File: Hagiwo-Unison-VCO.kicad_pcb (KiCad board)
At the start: 2 copper layers, 30 x 100 mm, 50 parts, among them J1 OSC2 VOL, J2 V/OCT, J3 Eurorack, J4 OUT, J5 Display, SW1 Wave, U1 XIAO_RA4M1, U2 AMS1117-5.0, U3 TL072, U4 TL072

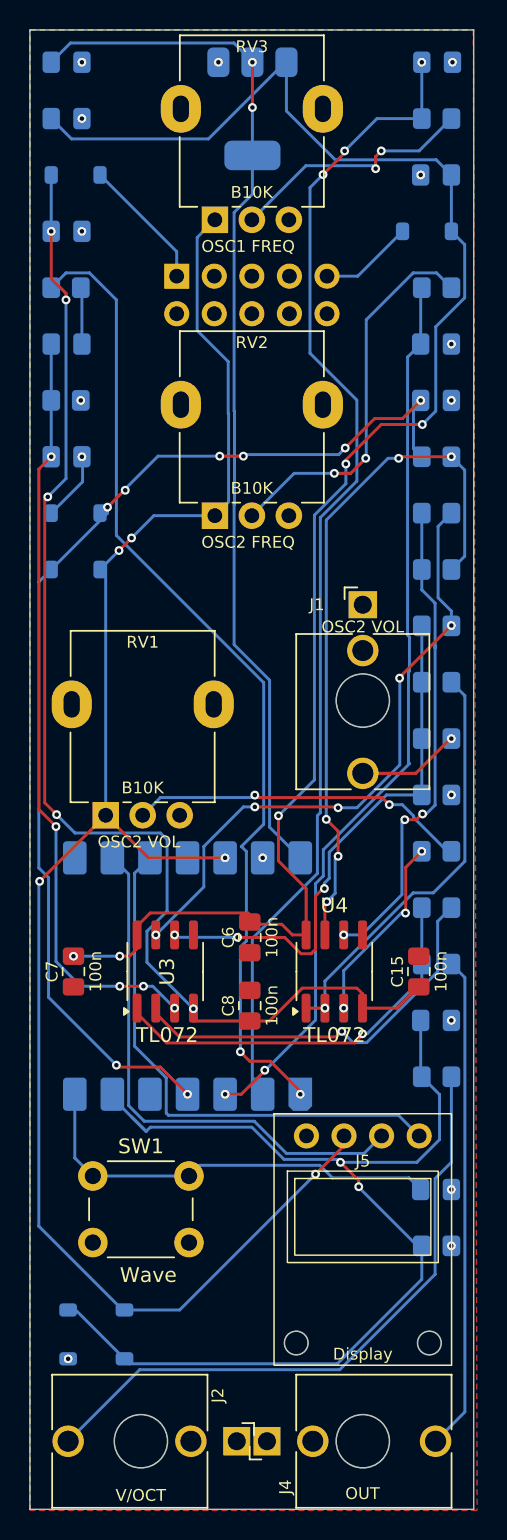
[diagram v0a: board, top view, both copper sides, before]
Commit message: add a pcb front panel
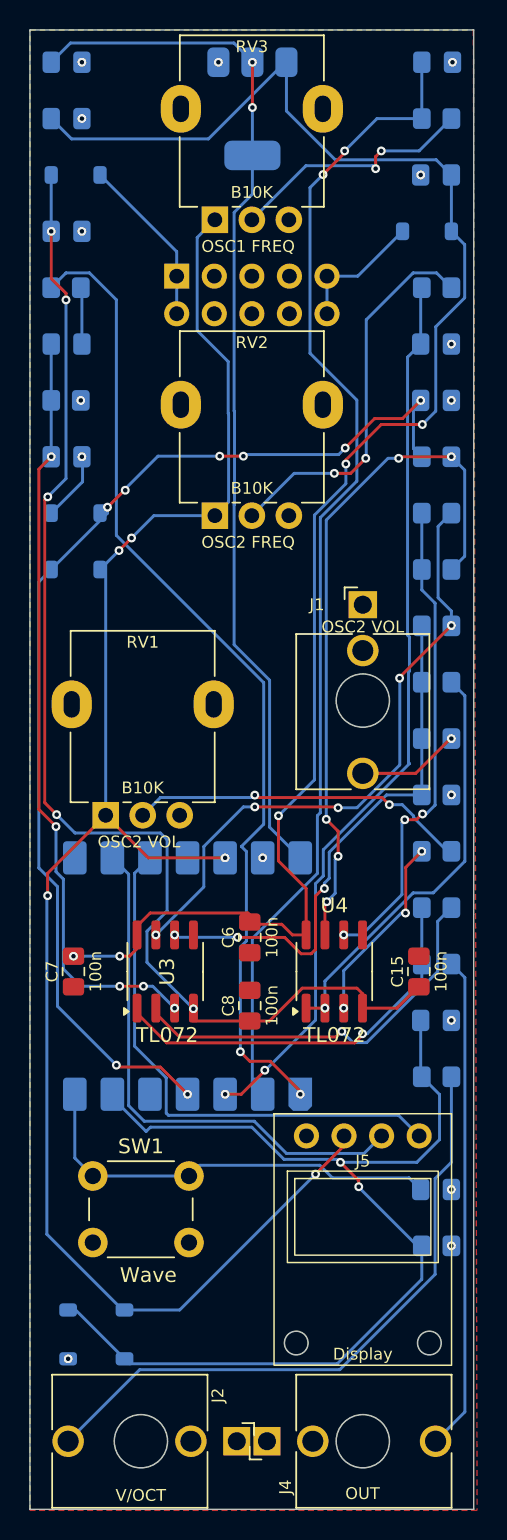
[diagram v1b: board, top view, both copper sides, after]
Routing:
- net Net-(D6-A): track 6.36 -> 8.90 mm
- net Net-(D5-K): track 8.99 -> 11.5 mm
- net /1V/OCT: track 73.2 -> 70.6 mm
- net +12V: track 112.9 -> 111.6 mm
- net +3.3V: track 114.7 -> 113.5 mm
- net /OSC1_FREQ: track 79.2 -> 78.2 mm, vias 3 -> 2
- net -12V: track 84.8 -> 83.9 mm
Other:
- board text added: "-12V"
